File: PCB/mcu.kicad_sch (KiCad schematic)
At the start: 36 parts

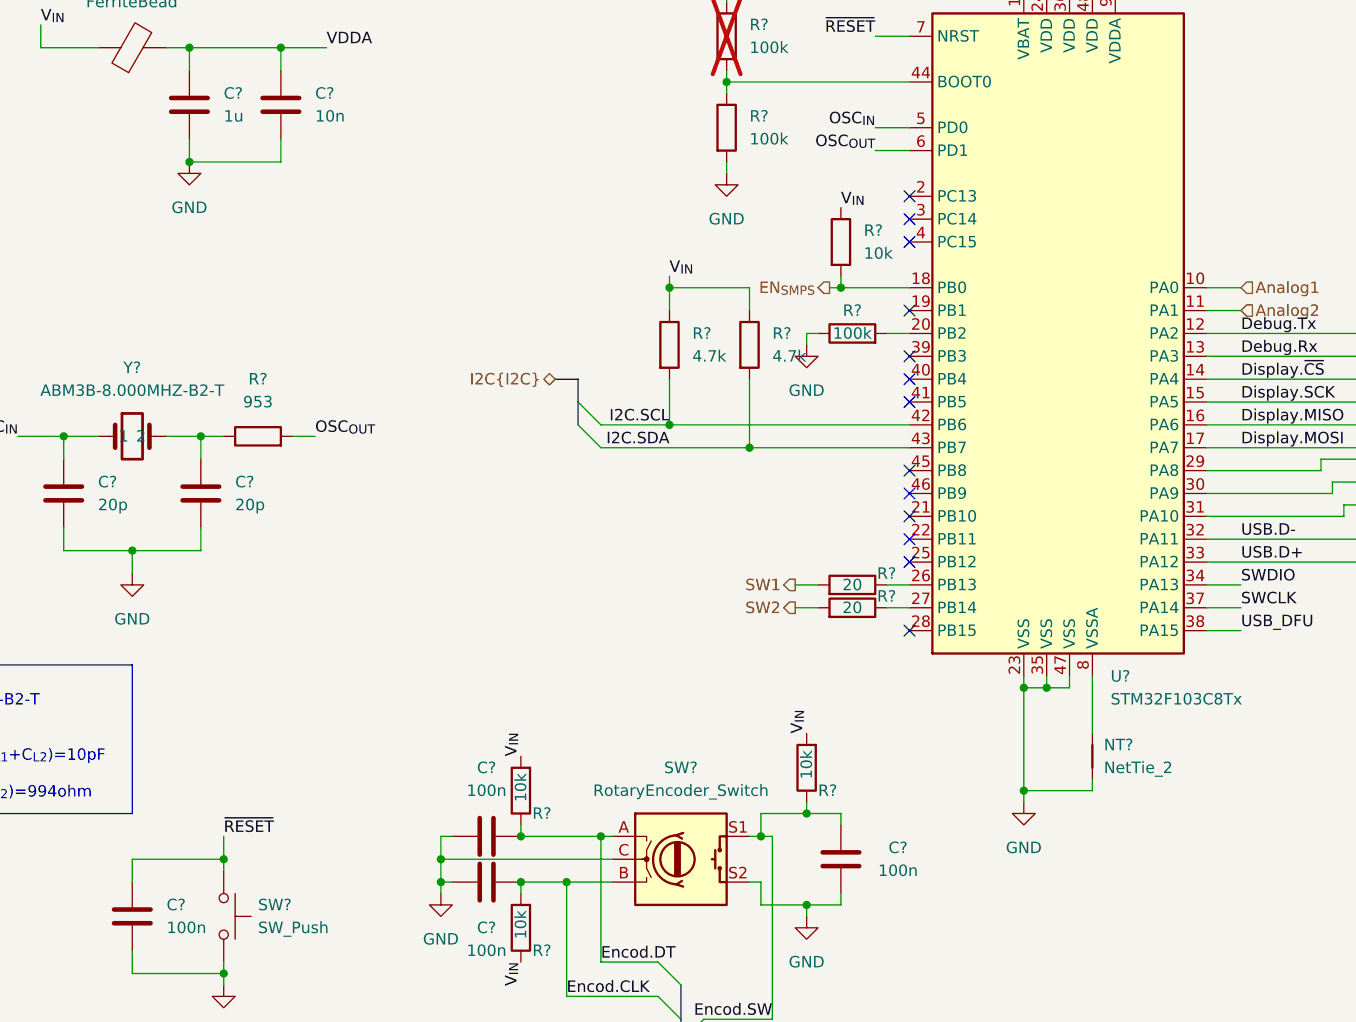
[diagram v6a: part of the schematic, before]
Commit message: ok dcdc and power switches
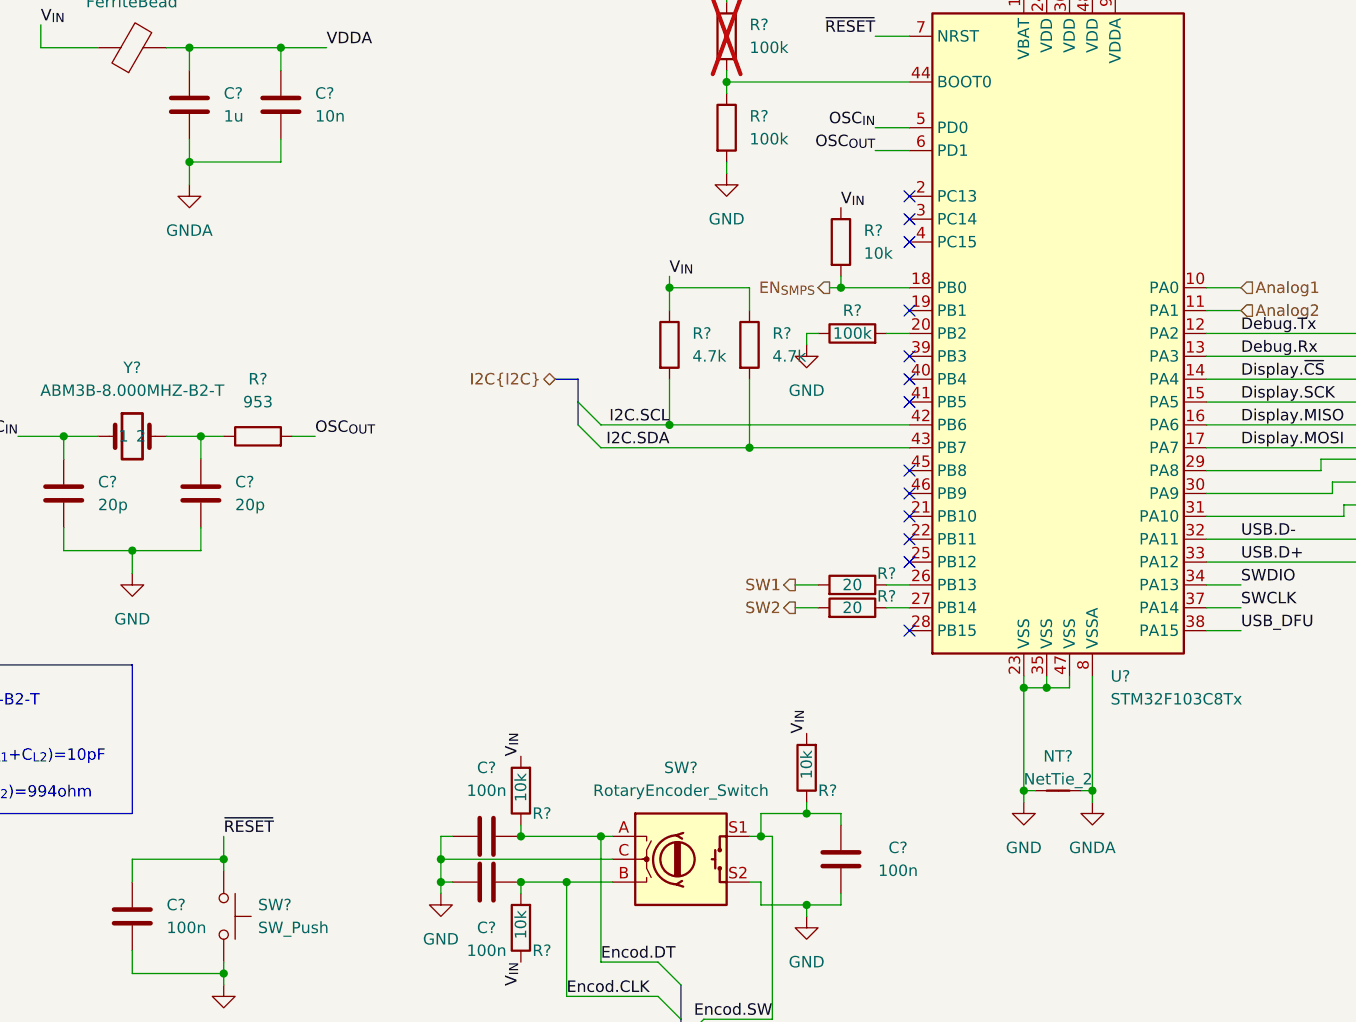
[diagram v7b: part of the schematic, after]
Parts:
- NT?: footprint (none) -> NetTie:NetTie-2_SMD_Pad0.5mm
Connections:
- net GND: now also NT?.2; no longer C?.2, C?.2, NT?.1
- net GNDA: now reaches U?.8 (VSSA)
- net GNDA: now also C?.2, C?.2, NT?.1; no longer NT?.2
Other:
- moved on the sheet: NT?

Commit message: add dac
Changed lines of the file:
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@@
-    (effects (font (size 1.27 1.27)) (justify left bottom))
-  )
-  (label "Display{SPI}" (at 186.69 102.87 0) (fields_autoplaced)
     (effects (font (size 1.27 1.27)) (justify left bottom))
   )
@@
     (effects (font (size 1.27 1.27)) (justify left))
   )
+  (hierarchical_label "Display{SPI}" (shape bidirectional) (at 186.69 102.87 0) (fields_autoplaced)
+    (effects (font (size 1.27 1.27)) (justify left))
+  )
